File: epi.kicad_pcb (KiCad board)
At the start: 2 copper layers, 12.7 x 23.1 mm, 28 parts, among them J1 Connector 1x12, J2 Connector 1x12, J3 Conn_01x05, J4 USB-C 2.0 mid-mount female co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, U1 ATmega32U4-M, Y1 Crystal_GND24_Small

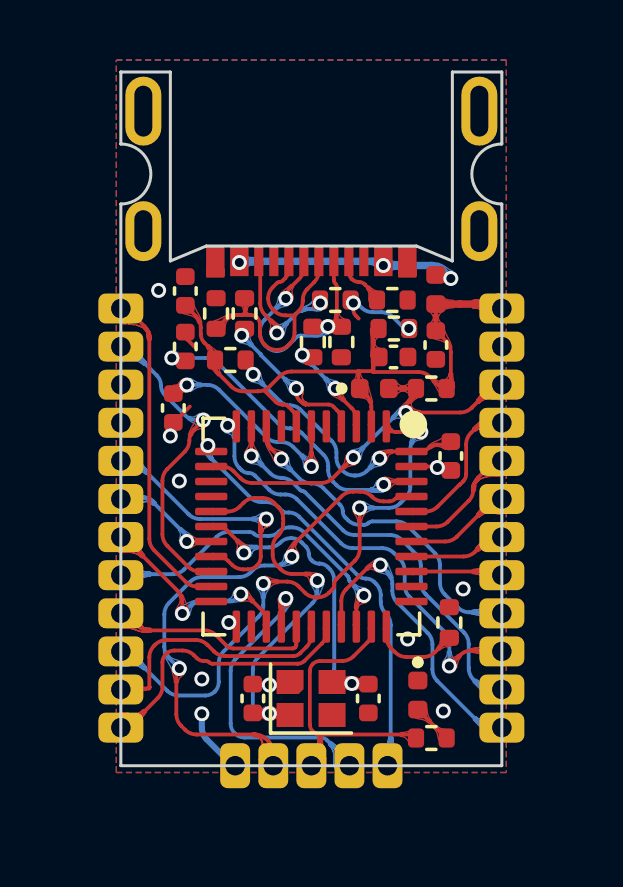
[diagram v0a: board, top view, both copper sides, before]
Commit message: fixed some dumb missed connection
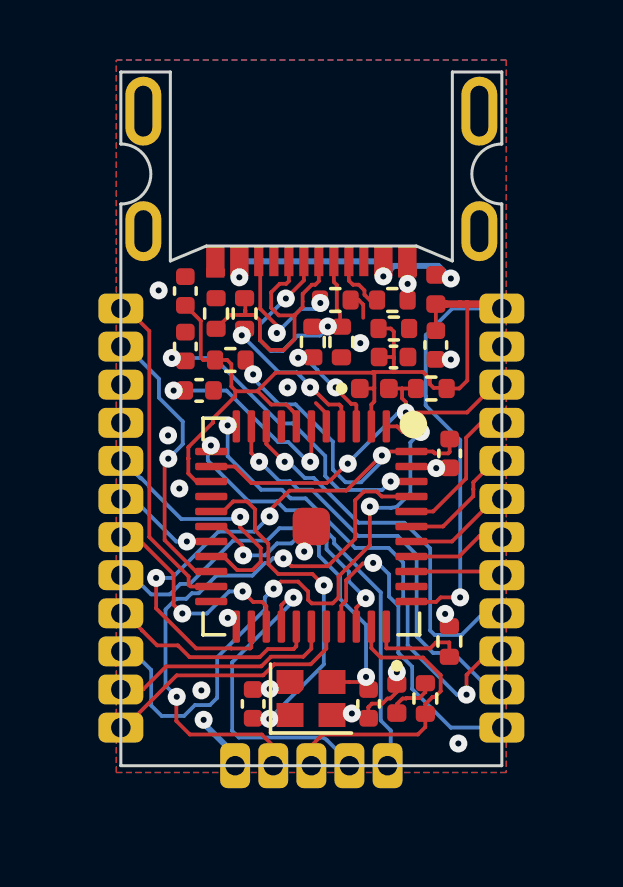
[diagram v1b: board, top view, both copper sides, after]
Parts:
- added ?: , , F.Cu at (104.3, 66.2)
- moved R8 1.33 mm to (108.1, 71.9), turned to -90 degrees
- moved C8 1.04 mm to (100.6, 61.6), turned to 180 degrees
- moved D2 0.71 mm to (107.2, 71.9)
- moved R7 0.63 mm to (108.9, 70.0)
- moved C5 0.18 mm to (106.2, 72.1)
- moved C6 0.18 mm to (102.4, 72.1)
- moved C2 0.10 mm to (109.0, 63.8)
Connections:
- net VBUS renamed +5V
- U1 pad 8: SS -> unconnected-(U1-Pad8)
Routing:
- net +5V: track 21.0 -> 42.4 mm, vias 0 -> 1
- net Net-(C2-Pad2): track 8.57 -> 24.5 mm, vias 2 -> 4
- net Net-(C6-Pad2): track 13.1 -> 11.1 mm
- net D7: track 18.6 -> 20.3 mm
- net D14/MISO: track 14.3 -> 15.9 mm
- net GND: track 8.31 -> 6.73 mm, vias 13 -> 17
- net D15/SCK: track 11.2 -> 12.5 mm
- net IO8: track 8.37 -> 7.26 mm
- net Net-(F1-Pad1): track 7.26 -> 8.29 mm
- net A5: track 18.1 -> 18.9 mm
- net IO10: track 9.88 -> 10.7 mm
- net D0/RX: track 10.3 -> 9.51 mm
- net Net-(J4-PadA7): track 9.57 -> 8.81 mm
- net D5: track 10.7 -> 11.3 mm
- net IO12: track 10.5 -> 11.1 mm
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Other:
- board text added: "CERN OHL-P"
- board text added: "Epi v1,3"
- board text removed: "Epi v1,2"

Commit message: bit of everything
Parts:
- added D+: TestPoint, TestPoint:TestPoint_Pad_D1.0mm, B.Cu at (102.5, 58.8)
- added D-: TestPoint, TestPoint:TestPoint_Pad_D1.0mm, B.Cu at (106.1, 58.7)
- moved R8 0.15 mm to (108.3, 72.0)
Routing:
- net GND: track 6.73 -> 8.63 mm
- net Net-(J4-PadA6): track 10.6 -> 11.9 mm, vias 0 -> 1
- net Net-(D2-Pad2): track 1.71 -> 2.61 mm
- net Net-(F1-Pad1): track 8.29 -> 7.52 mm
- net D14/MISO: track 15.9 -> 16.6 mm
- net IO12: track 11.1 -> 10.5 mm
- net D7: track 20.3 -> 19.8 mm
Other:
- board size 12.7 x 23.1 mm -> 16.7 x 24.8 mm
- board text added: "-D+"
- board text added: "Epi v1,4"
- board text removed: "Epi v1,3"

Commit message: updated pictures
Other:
- board size 16.7 x 24.8 mm -> 12.7 x 22.8 mm
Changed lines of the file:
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@@
   (gr_line (start 104.073705 64.296864) (end 104.088991 64.279593) (layer "B.SilkS") (width 0.18))
   (gr_line (start 104.477897 65.66537) (end 104.480601 65.6683) (layer "B.SilkS") (width 0.18))
+  (gr_line (start 95.99 57.9) (end 99.99 57.9) (layer "Dwgs.User") (width 0.05588))
+  (gr_line (start 108.94 76.16) (end 108.94 72.16) (layer "Dwgs.User") (width 0.05588))
+  (gr_line (start 99.69 76.16) (end 99.69 72.16) (layer "Dwgs.User") (width 0.05588))
+  (gr_line (start 108.69 57.9) (end 112.69 57.9) (layer "Dwgs.User") (width 0.05588))
   (gr_rect (start 98.94 72.15) (end 100.94 73.9) (layer "Dwgs.User") (width 0.15) (fill none))
   (gr_line (start 110.69 51.4) (end 110.69 53.65) (layer "Edge.Cuts") (width 0.1))
@@
   (gr_line (start 99.64 57.3365) (end 100.84 56.8365) (layer "Edge.Cuts") (width 0.1))
   (gr_line (start 100.84 56.8365) (end 107.84 56.8365) (layer "Edge.Cuts") (width 0.1))
-  (gr_line (start 95.99 57.9) (end 99.99 57.9) (layer "Edge.Cuts") (width 0.05588))
   (gr_arc (start 110.69 55.65) (mid 109.69 54.65) (end 110.69 53.65) (layer "Edge.Cuts") (width 0.1))
   (gr_arc (start 97.99 53.65) (mid 98.99 54.65) (end 97.99 55.65) (layer "Edge.Cuts") (width 0.1))
   (gr_line (start 109.04 51.4) (end 110.69 51.4) (layer "Edge.Cuts") (width 0.1))
   (gr_line (start 109.04 57.3365) (end 109.04 51.4) (layer "Edge.Cuts") (width 0.1))
-  (gr_line (start 108.94 76.16) (end 108.94 72.16) (layer "Edge.Cuts") (width 0.05588))
   (gr_line (start 110.69 74.16) (end 110.69 55.65) (layer "Edge.Cuts") (width 0.1))
-  (gr_line (start 99.69 76.16) (end 99.69 72.16) (layer "Edge.Cuts") (width 0.05588))
-  (gr_line (start 108.69 57.9) (end 112.69 57.9) (layer "Edge.Cuts") (width 0.05588))
   (gr_line (start 97.99 74.16) (end 110.69 74.16) (layer "Edge.Cuts") (width 0.1))
   (gr_line (start 97.99 55.65) (end 97.99 74.16) (layer "Edge.Cuts") (width 0.1))

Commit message: recommit
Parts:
- removed D1: Diode, Diode_SMD:D_0402_1005Metric
- removed FB1: Ferrite bead low-pass filter, Resistor_SMD:R_0402_1005Metric
- added R9: 5,1kΩ, Resistor_SMD:R_0402_1005Metric, F.Cu at (101.7, 60.6)
- renumbered D+ to TP1, D- to TP2
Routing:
- net RST: track 12.9 -> 12.1 mm
- net +5V: track 42.1 -> 41.6 mm

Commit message: fixed a wrong pin number
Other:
- board text added: "0"
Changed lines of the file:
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@@
     (effects (font (size 0.8 0.8) (thickness 0.16)) (justify mirror))
   )
-  (gr_text "2" (at 99.24 60.26) (layer "B.SilkS")
+  (gr_text "0" (at 99.24 60.26) (layer "B.SilkS")
     (effects (font (size 0.8 0.8) (thickness 0.16)) (justify mirror))
   )

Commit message: initial
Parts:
- removed ?: , 
- removed C1, C7: 100nf, Capacitor_SMD:C_0402_1005Metric
- removed R3: 10kΩ, Resistor_SMD:R_0402_1005Metric
- added C10: 100nF, Capacitor_SMD:C_0402_1005Metric, F.Cu at (106.6, 61.6)
- added C9: 100nF, Capacitor_SMD:C_0402_1005Metric, F.Cu at (99.7, 63.2)
- added D2: D_Schottky, DIY:SOD323_bättre, F.Cu at (107.7, 60.5)
- added FB1: Ferrite, Resistor_SMD:R_0402_1005Metric, F.Cu at (107.6, 59.0)
- added RV3: ESD protection varistor, Resistor_SMD:R_0402_1005Metric, F.Cu at (101.0, 59.0)
- C2: value 1µf -> 100nF
- C3, C4: value 22pf -> 100nF
- C5, C6: value 22pf -> 22pF
- C8: value 1µf -> 1µF
- R9: value 5,1kΩ -> 22Ω
- Y1: value Crystal_GND24_Small -> Crystal_GND24
- moved C3 13.9 mm to (108.9, 69.0), turned to 90 degrees
- moved R9 7.62 mm to (108.9, 63.0), turned to -90 degrees
- moved C4 5.30 mm to (103.4, 61.5), turned to 180 degrees
- moved R4 3.17 mm to (102.0, 59.0), turned to 90 degrees
- moved C8 2.96 mm to (103.4, 60.5), turned to 0 degrees
- moved RV2 1.77 mm to (102.9, 59.0), turned to -90 degrees
- moved R1 1.76 mm to (103.9, 59.0)
- moved R2 1.16 mm to (104.8, 59.0)
- moved RV1 1.16 mm to (105.8, 59.0)
- moved C2 1.15 mm to (108.9, 64.9)
- moved R7 1.05 mm to (108.2, 70.8), turned to 0 degrees
- moved F1 0.79 mm to (108.9, 59.0)
- moved R5 0.47 mm to (106.7, 59.0), turned to -90 degrees
- moved C6 0.40 mm to (102.0, 72.1), turned to 0 degrees
- moved D1 0.30 mm to (107.4, 72.2), turned to 90 degrees
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- renumbered D2 to D1
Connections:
- net IO10 renamed D10
- net IO11 renamed D11
- net IO12 renamed D12
- net IO8 renamed D8
- net IO9 renamed D9
- D1 pad 2: Net-(D2-Pad2) -> Net-(D1-Pad2)
- F1 pad 2: +5V -> Net-(D2-Pad2)
- J3 pad 3: IO13 -> D13
- J4 pad A4: Net-(F1-Pad1) -> Net-(J4-PadA4)
- J4 pad A9: Net-(F1-Pad1) -> Net-(J4-PadA4)
- R8 pad 1: Net-(D2-Pad2) -> D13
- R8 pad 2: IO13 -> Net-(D1-Pad2)
- U1 pad 32: IO13 -> D13
- U1 pad 42: Net-(C7-Pad1) -> unconnected-(U1-Pad42)
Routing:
- net +5V: track 41.6 -> 13.9 mm, vias 1 -> 4
- net Net-(C2-Pad2): track 24.4 -> 11.9 mm, vias 4 -> 0
- net D13: track 0.00 -> 11.6 mm, vias 0 -> 2
- net IO13: track 10.5 -> 0.00 mm
- net Net-(C7-Pad1): track 10.3 -> 0.00 mm, vias 2 -> 0
- net Net-(J4-PadA4): track 0.00 -> 10.3 mm, vias 0 -> 4
- net Net-(J4-PadA6): track 11.9 -> 4.00 mm
- net A5: track 19.0 -> 12.0 mm, vias 2 -> 1
- net D7: track 19.8 -> 13.3 mm, vias 3 -> 1
- net Net-(F1-Pad1): track 7.52 -> 1.31 mm, vias 3 -> 0
- net GND: track 8.63 -> 2.91 mm, vias 17 -> 8
- net Net-(J4-PadA7): track 8.79 -> 3.33 mm, vias 2 -> 1
- net Net-(C8-Pad2): track 6.67 -> 2.54 mm, vias 2 -> 0
- net D2/SDA: track 8.63 -> 5.41 mm, vias 1 -> 0
- net Net-(J4-PadB5): track 4.19 -> 1.52 mm, vias 2 -> 0
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- added copper zone on In1.Cu, net +5V
- added copper zone on In2.Cu, net GND
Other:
- copper layers 2 -> 4
- board text added: "Epi v1,2,0"
- board text removed: "Epi v1,4"
- board text removed: "JLCJLCJLCJLC"
- board text removed: "Made in the EU"
- board text removed: "RoHS"
